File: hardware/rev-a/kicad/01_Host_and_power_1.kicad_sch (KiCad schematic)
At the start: 16 parts, among them J1 CoreS3 M5-Bus, J2 5V external 2A, U11 MCW03-05D12

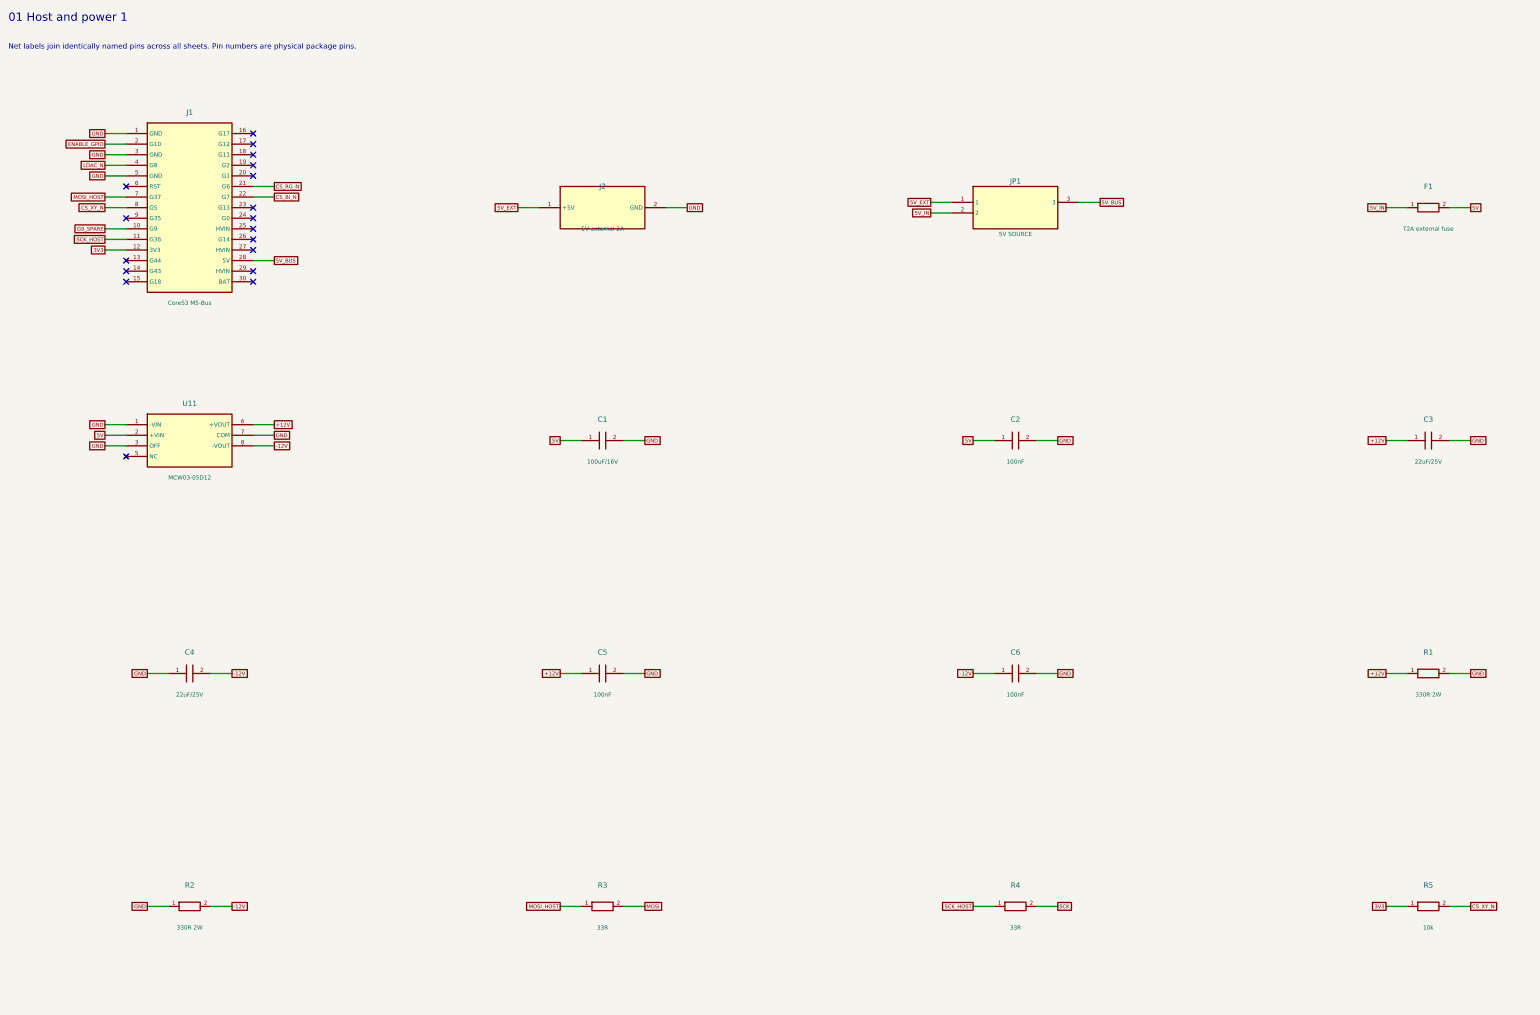
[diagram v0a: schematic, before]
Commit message: Redraw Rev.A schematics with functional blocks and explicit wiring
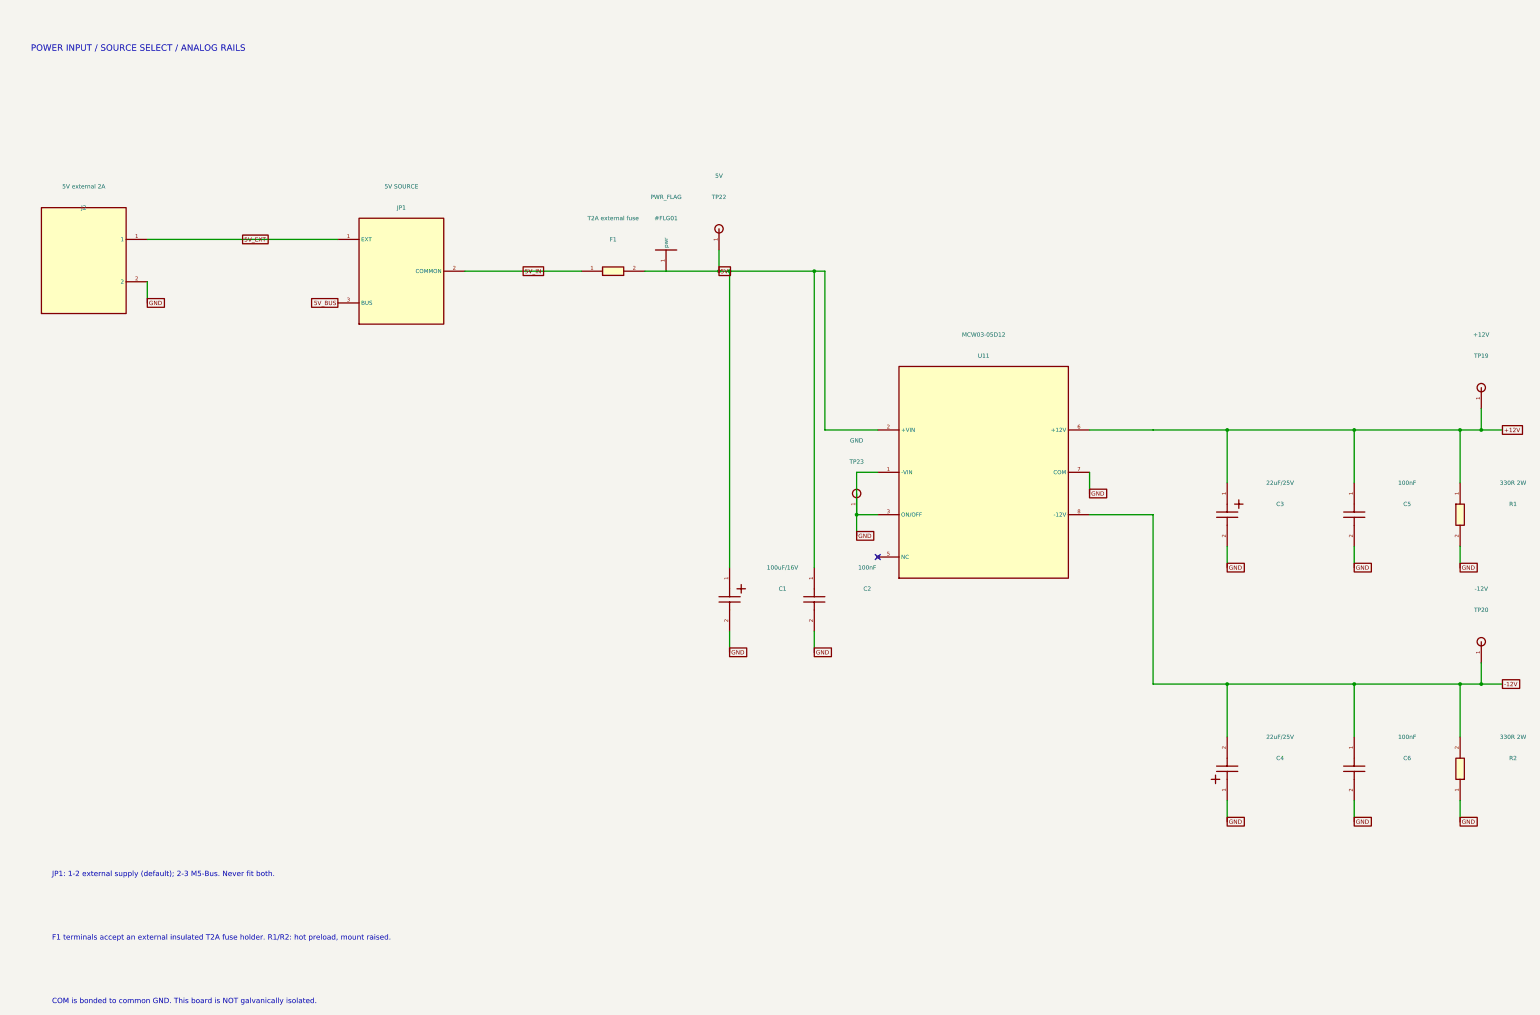
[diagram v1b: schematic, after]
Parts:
- removed J1: CoreS3 M5-Bus, RevA:M5Bus_CoreS3_TypeA, symbol RevA:Bus_J1
- removed R3, R4: 33R, RevA:R_Axial_DIN0207_L6.3mm_D2.5mm_P10.16mm_Horizontal, symbol RevA:R
- removed R5: 10k, RevA:R_Axial_DIN0207_L6.3mm_D2.5mm_P10.16mm_Horizontal, symbol RevA:R
- added TP19: +12V, RevA:TestPoint_THTPad_D2.0mm_Drill1.0mm, symbol RevA:TP
- added TP20: -12V, RevA:TestPoint_THTPad_D2.0mm_Drill1.0mm, symbol RevA:TP
- added TP22: 5V, RevA:TestPoint_THTPad_D2.0mm_Drill1.0mm, symbol RevA:TP
- added TP23: GND, RevA:TestPoint_THTPad_D2.0mm_Drill1.0mm, symbol RevA:TP
- J2: symbol RevA:Conn_J2 -> RevA:Part_J2
- JP1: symbol RevA:Conn_JP1 -> RevA:Part_JP1
- U11: symbol RevA:DCDC -> RevA:Part_U11
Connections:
- net +12V: now also TP19.1
- net -12V: now also TP20.1
- net 5V: now also TP22.1
- net GND: now also TP23.1
- no-connect marks 18 -> 1
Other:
- note added: "COM is bonded to common GND. This board is NOT galvanically isolated."
- note added: "F1 terminals accept an external insulated T2A fuse holder. R1/R2: hot preload, mount raised."
- note added: "JP1: 1-2 external supply (default); 2-3 M5-Bus. Never fit both."
- note added: "POWER INPUT / SOURCE SELECT / ANALOG RAILS"
- note removed: "01 Host and power 1"
- note removed: "Net labels join identically named pins across all sheets. Pin numbers are physical package pins."
- company: CoreS3 ILDA evaluation -> (none)
- title: 01_Host_and_power_1 -> 01 / 5V input and +/-12V supply
- moved on the sheet: J2, JP1, U11
